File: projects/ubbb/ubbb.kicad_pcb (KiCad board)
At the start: 2 copper layers, 14 parts, among them CON1 USB-MINI-B, IC1 ATMEGA328-P, P1 CONN_7, P2 CONN_4, P3 CONN_14, X1 CRYSTAL_RESONATOR

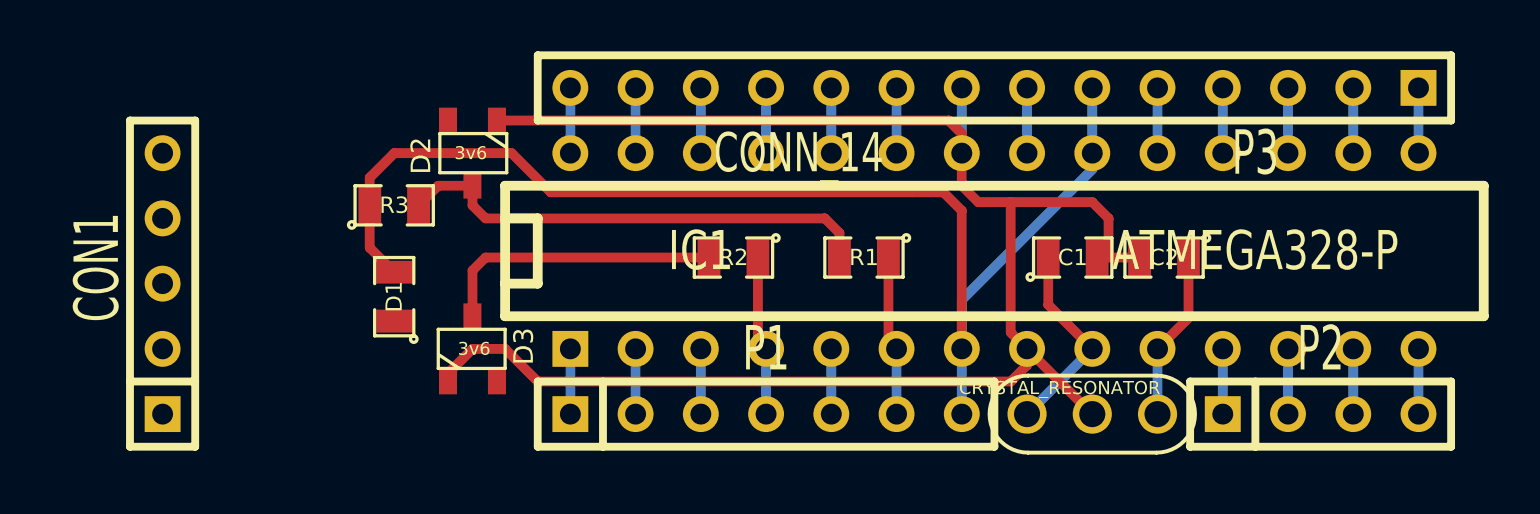
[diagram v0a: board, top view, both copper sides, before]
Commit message: Added micro USB B connector
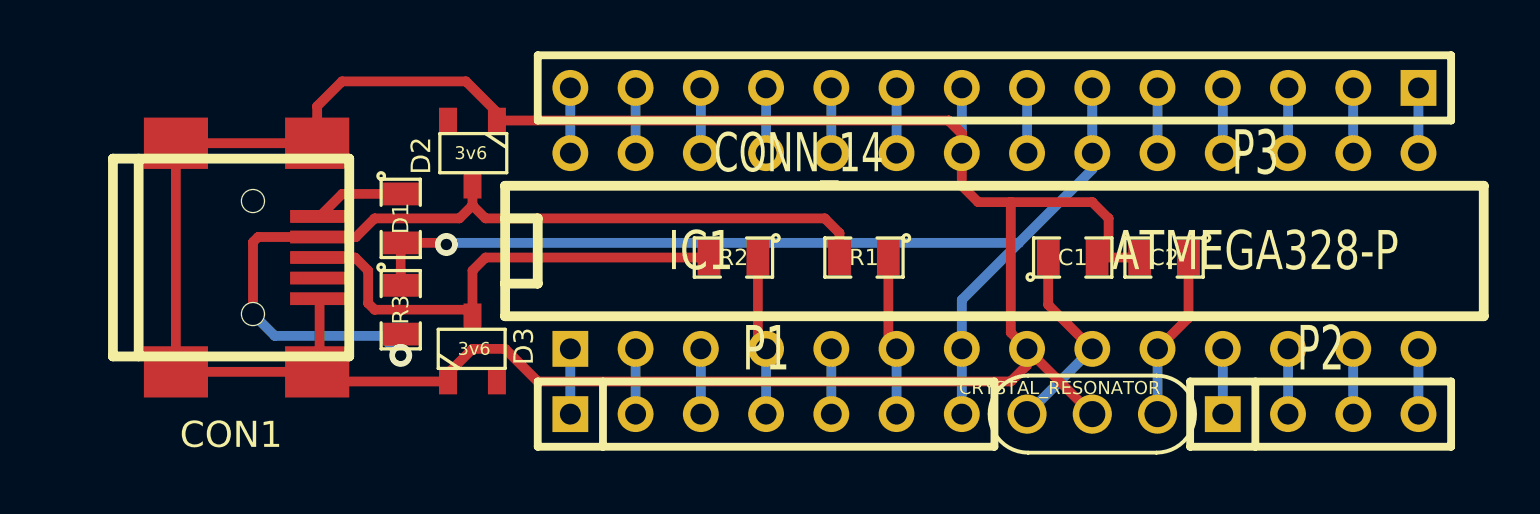
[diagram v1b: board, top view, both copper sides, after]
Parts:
- CON1: footprint SIL-5 -> USB_MINI_B
- moved R3 4.07 mm to (30.2, 34.0), turned to 270 degrees
- moved D1 3.06 mm to (30.2, 30.5), turned to 270 degrees
- moved CON1 2.68 mm to (23.6, 32.0), turned to 0 degrees
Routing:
- net GND: track 68.3 -> 106.0 mm
- net /D-: track 18.9 -> 35.6 mm, vias 0 -> 1
- net VCC: track 48.6 -> 40.6 mm, vias 0 -> 1
- net /D+: track 11.2 -> 18.8 mm
- net /VBUS: track 0.00 -> 3.52 mm
